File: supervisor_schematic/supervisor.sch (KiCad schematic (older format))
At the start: 32 parts, among them J1 Conn_01x08, J16 Conn_01x06_Female, J17 Conn_01x04_Female, J2 Conn_01x05, J3 Conn_01x02, SW1 SW_Push, SW2 SW_Push, SW3 SW_Push, U1 74HC14, U2 RFM9-LoRa-Radio

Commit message: v2 almost done
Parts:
- added Q1, Q2: BSS138, Package_TO_SOT_SMD:SOT-23, symbol Transistor_FET:BSS138
- added R10, R11, R12, R13: 10K, Resistor_SMD:R_0805_2012Metric_Pad1.15x1.40mm_HandSolder, symbol Device:R
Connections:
- net +3V3: now also VR1.3 (VOUT), Q1.1 (G), Q2.1 (G), R10.1, R11.1
- net +5V: now also VR1.1 (VIN), R12.1, R13.1
- net GND: now also VR1.2 (GND)
- net SCL: now also Q1.2 (S), R10.2; no longer J17.4 (Pin_4)
- net SD0: now also U2.6 (MISO); no longer J3.1 (Pin_1)
- net SD1: now also U2.7 (MOSI); no longer J3.2 (Pin_2)
- net SD2: now also J3.1 (Pin_1); no longer U2.6 (MISO)
- net SD3: now also J3.2 (Pin_2); no longer U2.7 (MOSI)
- net SDA: now also Q2.2 (S), R11.2; no longer J17.3 (Pin_3)
- new net: J17.3 (Pin_3), Q2.3 (D), R13.2
- new net: J17.4 (Pin_4), Q1.3 (D), R12.2
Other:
- moved on the sheet: J1, J2, J3, VR1

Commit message: ordered
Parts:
- removed J1: Conn_01x08, Connector_PinHeader_2.54mm:PinHeader_1x08_P2.54mm_Vertical, symbol Connector_Generic:Conn_01x08
- removed J16: Conn_01x06_Female, Connector_PinHeader_2.54mm:PinHeader_1x06_P2.54mm_Vertical, symbol Connector:Conn_01x06_Female
- removed J3: Conn_01x02, Connector_PinHeader_2.54mm:PinHeader_1x02_P2.54mm_Vertical, symbol Connector_Generic:Conn_01x02
- added C4: 1u, Capacitor_SMD:C_0805_2012Metric_Pad1.15x1.40mm_HandSolder, symbol Device:CP1
- added J1: Conn_01x06, Connector_PinHeader_2.54mm:PinHeader_1x06_P2.54mm_Vertical, symbol Connector_Generic:Conn_01x06
- added J3: Conn_01x04, Connector_PinHeader_2.54mm:PinHeader_1x04_P2.54mm_Vertical, symbol Connector_Generic:Conn_01x04
- added J4: Conn_01x07_Female, Connector_PinHeader_2.54mm:PinHeader_1x07_P2.54mm_Vertical, symbol Connector:Conn_01x07_Female
- added Q3, Q4: MMBT2222, Noggin:SOT95P240X114-3N, symbol Noggin:MMBT2222
- added R14: 10K, Resistor_SMD:R_0805_2012Metric_Pad1.15x1.40mm_HandSolder, symbol Device:R
- added R15, R16: 10k, Resistor_SMD:R_0805_2012Metric_Pad1.15x1.40mm_HandSolder, symbol Device:R
- added SW4: SW_Push, Button_Switch_THT:SW_PUSH_6mm, symbol Switch:SW_Push
- D1, D2, D3: footprint Capacitor_SMD:C_0805_2012Metric_Pad1.15x1.40mm_HandSolder -> Noggin:0805_LED_Extended
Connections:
- net +3V3: now also VR1.1 (VIN), R14.1; no longer VR1.3 (VOUT)
- net +5V: now also VR1.3 (VOUT); no longer VR1.1 (VIN)
- net CLK: now also J1.4 (Pin_4); no longer U2.5 (SCK)
- net CS: now also ANT1.23 (IO15); no longer ANT1.19 (CMD)
- net GND: now also C4.2, J4.6 (Pin_6)
- net GPIO36: now also J2.1 (Pin_1)
- net GPIO39: now also J2.2 (Pin_2)
- net IO0: now also C4.1, Q3.3, R14.2, SW4.1
- net IO2: now also J3.4 (Pin_4); no longer J2.5 (Pin_5)
- net IO23: now also J3.1 (Pin_1); no longer J2.1 (Pin_1)
- net IO27: now also J2.5 (Pin_5)
- net IO34: now also J2.3 (Pin_3)
- net IO35: now also J2.4 (Pin_4)
- net IO4: now also J3.3 (Pin_3); no longer J2.4 (Pin_4)
- net IO5: now also J3.2 (Pin_2); no longer J2.3 (Pin_3)
- net RESET: now also Q4.3
- net RX: now also J4.3 (Pin_3)
- net SD0: now also J1.5 (Pin_5); no longer U2.6 (MISO)
- net SD1: now also J1.6 (Pin_6); no longer U2.7 (MOSI)
- net SD2: now also J1.1 (Pin_1)
- net SD3: now also J1.2 (Pin_2)
- net TX: now also J4.2 (Pin_2)
- net at R5.2: now also ANT1.31 (IO19); no longer ANT1.23 (IO15)
- net IO12 renamed MISO
- net MISO: now also U2.6 (MISO)
- net IO13 renamed MOSI
- net MOSI: now also U2.7 (MOSI)
- net IO14 renamed SCLK
- net SCLK: now also U2.5 (SCK)
- removed net IO19: ANT1.31 (IO19), J2.2 (Pin_2)
- new net: Q3.1, R15.1
- new net: Q4.1, R16.2
- new net CMD: ANT1.19 (CMD), J1.3 (Pin_3)
- new net DTR: J4.1 (Pin_1), Q3.2, R16.1
- new net RTS: J4.7 (Pin_7), Q4.2, R15.2
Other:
- note added: "Programming Header\n"
- moved on the sheet: LS1, R5, VR1

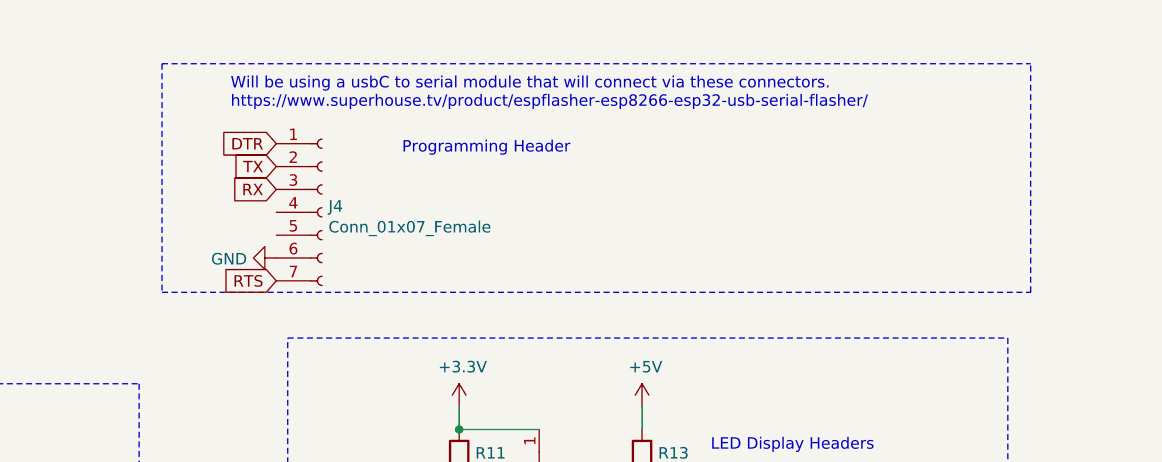
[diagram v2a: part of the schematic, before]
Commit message: supervisor schem
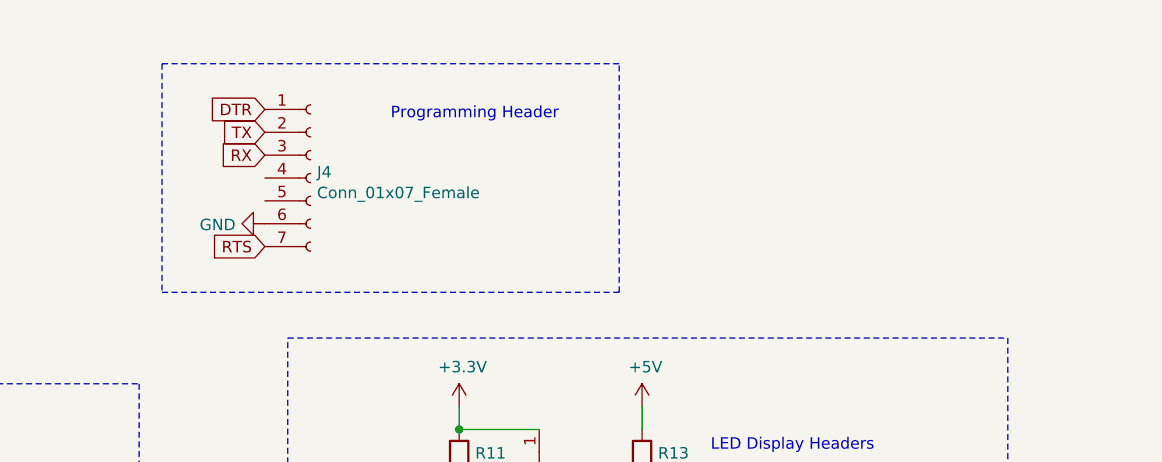
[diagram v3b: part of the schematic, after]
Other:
- note removed: "Will be using a usbC to serial module that will connect via these connectors. \nhttps://www.superhouse.tv/product/espflasher-esp8266-esp32-usb-serial-flasher/"
- moved on the sheet: J4
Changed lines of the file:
@@
 Text Notes 1500 4950 0    50   ~ 0
 Button Debouncing
-Text Notes 7450 900  0    50   ~ 0
-Will be using a usbC to serial module that will connect via these connectors. \nhttps://www.superhouse.tv/product/espflasher-esp8266-esp32-usb-serial-flasher/
-Text Notes 8200 1100 0    50   ~ 0
+Text Notes 8150 950  0    50   ~ 0
 Programming Header
-Text GLabel 7650 1050 0    50   Input ~ 0
+Text GLabel 7600 900  0    50   Input ~ 0
 DTR
-Text GLabel 7650 1250 0    50   Input ~ 0
+Text GLabel 7600 1100 0    50   Input ~ 0
 RX
-Text GLabel 7650 1150 0    50   Input ~ 0
+Text GLabel 7600 1000 0    50   Input ~ 0
 TX
 $Comp
 L power:GND #PWR0114
 U 1 1 6232C2D0
-P 7650 1550
-F 0 "#PWR0114" H 7650 1300 50  0001 C CNN
-F 1 "GND" V 7655 1422 50  0000 R CNN
-F 2 "" H 7650 1550 50  0001 C CNN
-F 3 "" H 7650 1550 50  0001 C CNN
-	1    7650 1550
+P 7600 1400
+F 0 "#PWR0114" H 7600 1150 50  0001 C CNN
+F 1 "GND" V 7605 1272 50  0000 R CNN
+F 2 "" H 7600 1400 50  0001 C CNN
+F 3 "" H 7600 1400 50  0001 C CNN
+	1    7600 1400
 	0    1    1    0
 $EndComp
@@
 	-1   0    0    1
 $EndComp
-Wire Notes Line
-	7150 700  10950 700
 Text GLabel 10650 4700 0    50   Input ~ 0
 IO23
@@
 Text Notes 9550 2400 0    50   ~ 0
 LED Display Headers\n
-Wire Notes Line
-	10950 1700 10950 700
-Wire Notes Line
-	7150 1700 10950 1700
 $Comp
 L Connector:Conn_01x04_Female J17
@@
 L Connector:Conn_01x07_Female J4
 U 1 1 623A2C66
-P 7850 1350
-F 0 "J4" H 7878 1376 50  0000 L CNN
-F 1 "Conn_01x07_Female" H 7878 1285 50  0000 L CNN
-F 2 "Connector_PinHeader_2.54mm:PinHeader_1x07_P2.54mm_Vertical" H 7850 1350 50  0001 C CNN
-F 3 "~" H 7850 1350 50  0001 C CNN
-	1    7850 1350
-	1    0    0    -1
-$EndComp
-Text GLabel 7650 1650 0    50   Input ~ 0
+P 7800 1200
+F 0 "J4" H 7828 1226 50  0000 L CNN
+F 1 "Conn_01x07_Female" H 7828 1135 50  0000 L CNN
+F 2 "Connector_PinHeader_2.54mm:PinHeader_1x07_P2.54mm_Vertical" H 7800 1200 50  0001 C CNN
+F 3 "~" H 7800 1200 50  0001 C CNN
+	1    7800 1200
+	1    0    0    -1
+$EndComp
+Text GLabel 7600 1500 0    50   Input ~ 0
 RTS
+Wire Notes Line
+	7150 1700 9150 1700
+Wire Notes Line
+	9150 1700 9150 700
+Wire Notes Line
+	9150 700  7150 700
 $EndSCHEMATC
